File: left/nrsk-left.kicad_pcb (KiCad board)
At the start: 2 copper layers, 172.6 x 133.6 mm, 137 parts, among them J1 PJ-320D, J2 USB-C, J3 OLED 128x32, SW1 Esc, SW10 1, SW11 2, SW12 3, SW13 4, SW14 5, SW15 6, SW16 16, SW17 Tab, SW18 Q, SW19 W, SW2 F1, SW20 E, SW21 R, SW22 T, SW23 23, SW24 Ctrl, SW25 A, SW26 S, SW27 D, SW28 F, SW29 G, SW3 F2, SW30 30, SW31 Shift, SW32 Z, SW33 X, SW34 C, SW35 V, SW36 B, SW37 37, SW38 Ctrl, SW39 Opt, SW4 F3, SW40 Cmd, SW41 Space, SW42 Space, SW43 Space, SW44 44, SW5 F4, SW6 F5, SW7 F6, SW8 8, SW9 `, U1 RP2040, U2 USBLC6-2SC6, U4 AP2112K-3.3, U5 W25Q128JVS, Y1 12MHz

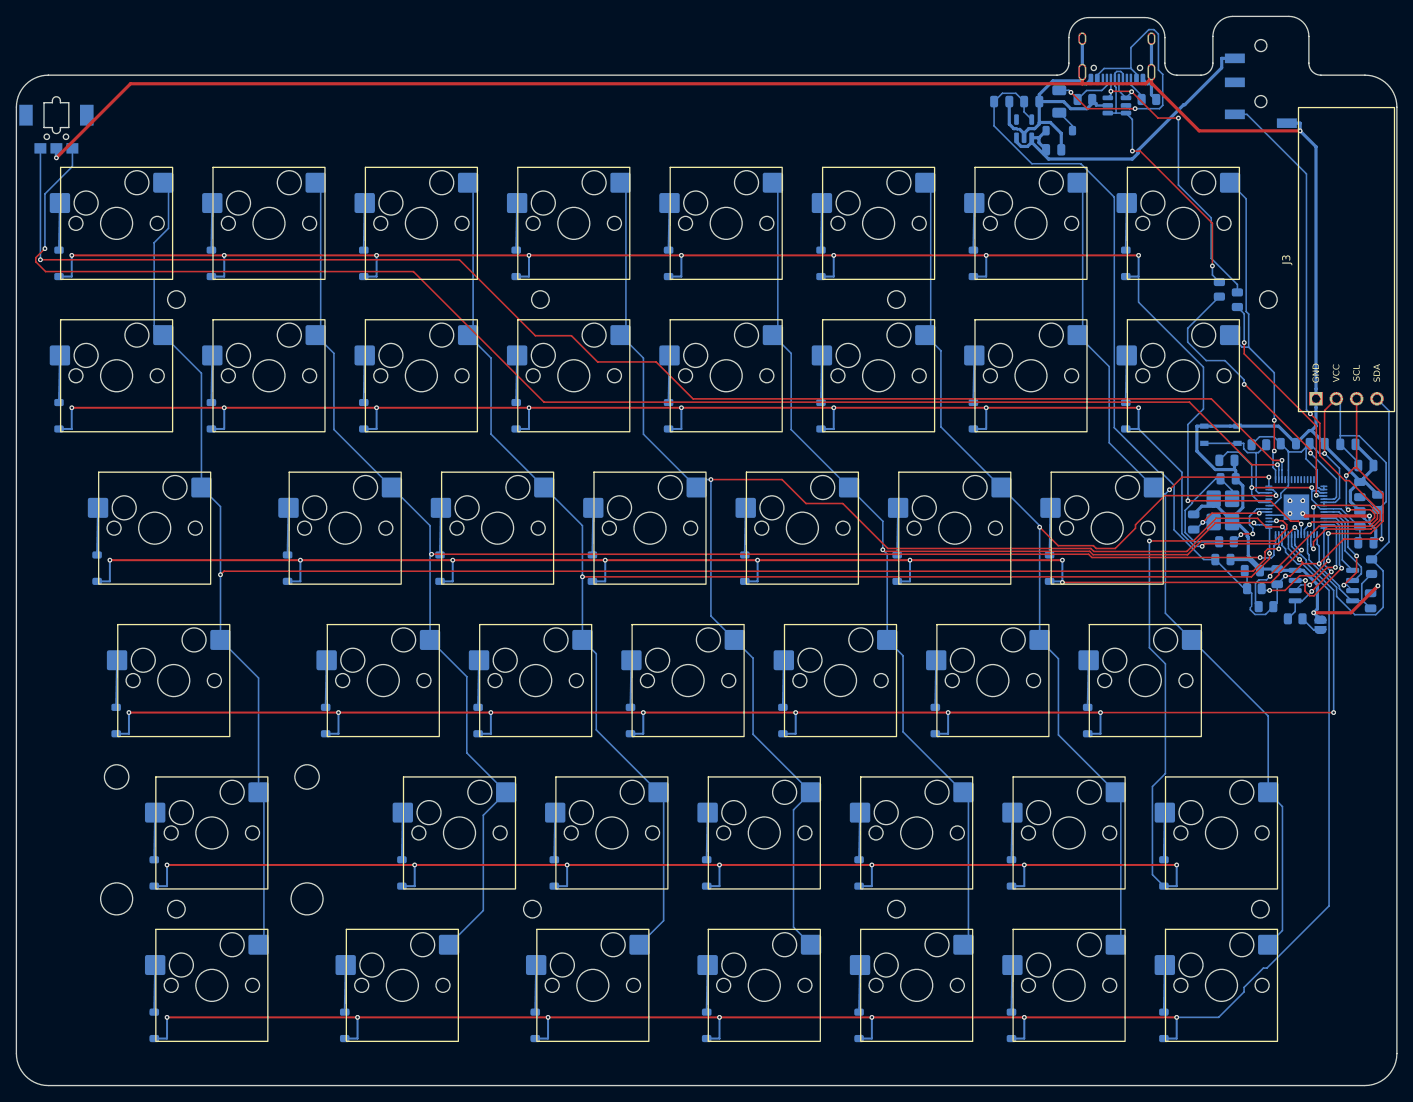
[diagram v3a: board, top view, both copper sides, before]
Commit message: GND copper on both faces of both boards, stitched with vias
- route.py pour(), run after routing and cleanup: a GND zone over the whole board on F.Cu and B.Cu
  (0.3 mm to other nets, 0.25 mm minimum width; the mounting-hole keepouts still win). The routed
  GND tracks stay. SMD pads join solidly (JLC reflows them), through-hole pads get thermal spokes,
  except the USB-C shell legs (JLC solders them; solid to GND)
- Stitching vias (0.6 / 0.3 mm) on a 5 mm grid, plus a 1.25 mm grid wherever no via is within
  3.75 mm, so narrow copper boxed in by tracks gets one too; a via goes only where its ring lies in
  the copper of both faces and its drill keeps 0.5 mm from other holes. Islands still unconnected are
  removed, with any via standing in them. Left 850, right ~966 stitching vias
- Applied to the routed boards (placement and routing unchanged, so the JLC CPL is unchanged);
  future builds pour after each routing pass
- DRC: 5 per side (silk at the connector mouths), down from 8: the 3 RP2040 thermal-pad vias now
  reach the F.Cu copper. 0 unconnected, 0 parity issues, ERC 0. Gerbers, PDFs, 3D viewer, assembly
  guide and board images regenerated
- README: board spec, how the copper is poured, DRC note

Co-Authored-By: Claude Opus 5.5 <noreply@anthropic.com>
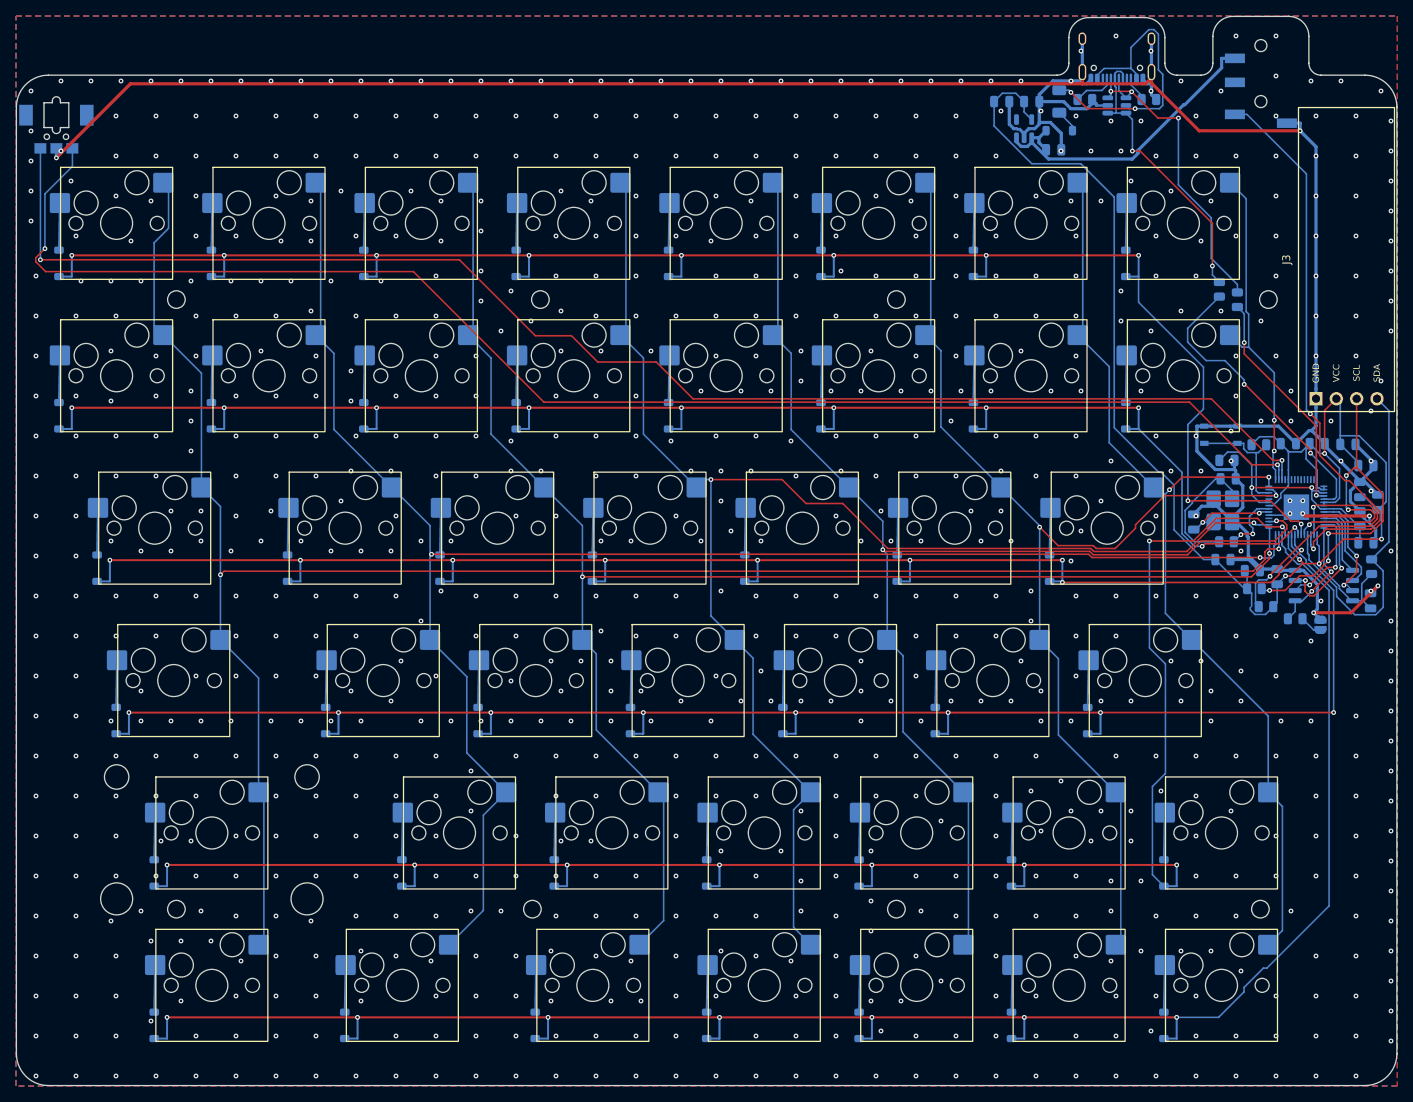
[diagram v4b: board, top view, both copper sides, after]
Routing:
- net GND: vias 9 -> 859
- added copper zone on B.Cu, net GND
- added copper zone on F.Cu, net GND

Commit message: Split link over USB-C instead of TRRS, so both port openings line up
The TRRS jack (PJ-320D) hung 5.0 mm under the PCB with its axis 2.5 mm down,
while the USB-C shell's axis is 1.63 mm down, so the two openings in the back
wall sat at different heights. The link now uses a second HRO TYPE-C-31-M-12:
same part, same height, same rounded slot.

- J1 is a USB-C receptacle: VBUS = VCC, D+ (A6/B6) = DATA (GP1), GND; D- and
  CC open, so a host or charger plugged in by mistake keeps VBUS off.
- PCB / case / JLC / BOM generators: the 'trrs' connector kind becomes 'link'
  and is handled like the host USB-C; PJ-320D footprint, model and JLC fix go.
- BOM: 4 USB-C receptacles, a C-C data cable for the link; one fewer
  Extended JLC part (9).
- Docs: README, ordering, pre-order checklist, thumbwheel check, assembly
  guide updated (pinout, which port is which, data cable required).
- Rebuilt: schematics, PCBs (0 unconnected, 0 parity issues, 4 silk warnings
  per side), fab outputs, case, BOM, JLC files, KiCad doc images.

Co-Authored-By: Claude Opus 5.5 <noreply@anthropic.com>
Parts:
- J1: value PJ-320D -> USB-C; footprint Connector_Audio:Jack_3.5mm_PJ320D_Horizontal -> Connector_USB:USB_C_Receptacle_HRO_TYPE-C-31-M-12
- moved J1 4.58 mm to (182.6, 17.5), turned to 0 degrees
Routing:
- net /SCL: track 57.6 -> 34.2 mm, vias 6 -> 2
- net /ROW3: track 204.8 -> 186.4 mm
- net /3V3: track 207.2 -> 192.5 mm
- net /SDA: track 44.6 -> 30.8 mm, vias 0 -> 2
- net /VBUS: track 38.5 -> 25.2 mm, vias 2 -> 3
- net /D-: track 28.6 -> 41.3 mm
- net /HAND: track 34.5 -> 23.5 mm, vias 2 -> 0
- net /ROW5: track 230.3 -> 240.9 mm, vias 7 -> 9
- net /VFUSE: track 2.93 -> 11.2 mm
- net /ROW0: track 216.2 -> 223.6 mm
- net VCC: track 39.9 -> 47.2 mm, vias 0 -> 2
- net /DATA: track 71.7 -> 78.5 mm
- net /COL4: track 161.2 -> 155.9 mm
- net /QSPI_SD0: track 8.89 -> 14.2 mm, vias 0 -> 2
- net /XIN: track 11.8 -> 17.0 mm
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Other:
- board size 172.6 x 133.6 mm -> 172.6 x 133.5 mm

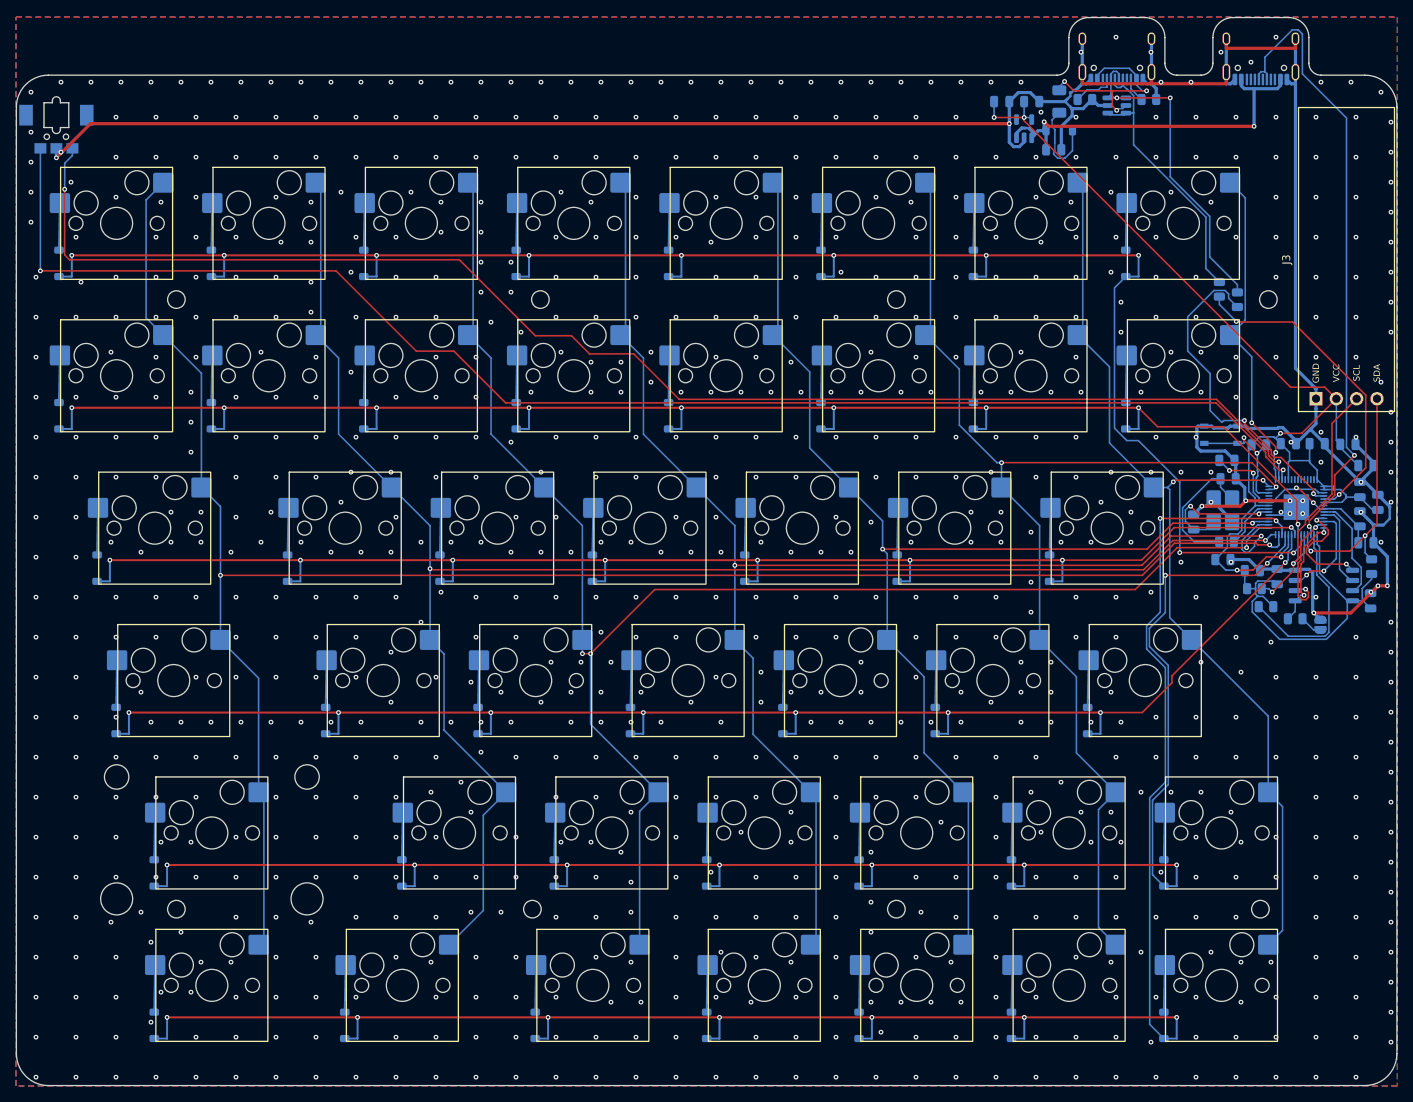
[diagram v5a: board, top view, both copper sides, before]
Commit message: Remove the blank inner key column on both halves; even plate band round the OLED cover
KLE: the unlabeled keys of the inner column go (left 8, 16, 23, 30, 37, 44; right 71, 73, 75, 77, 79, 81), so
the halves have 38 + 42 = 80 keys. The right "\" key now sits in its own row (row 2, col 7) and the remap goes;
the left's COL7 stays unconnected in the schematic.

The gap is closed: the right board moves its keys one unit in (key_shift +1 u, width -1 u). The left board is
sized from its row 0-1 keycaps: COVER_FRAME + the OLED cover (window + 5 mm each side) + COVER_FRAME, less the
case wall, so it narrows by 15.4 mm instead of a full unit.

The OLED's half-mirror cover is now laid out from the plate band round it: 3.5 mm to the case outline (top and
inner edge), to the nearest row 0-1 keycaps, and to the row-2 keycap line below, on both halves; the corner at the
case corner is concentric with it (R9), the others R2. The OLED stays at its height: its display glass, 3 mm
toward the module's top, lands at the cover's centre, and higher up the module would leave the board's rounded
corner and meet the link USB-C's shield pins. make_case checks the band against keycaps and the outline.

Sizes: boards 157.1 / 180.5 x 126.3 mm, cases 174.1 / 197.5 x 143.3 mm. The drum stays centred on Backspace.
Docs (README, ordering, pre-order checklist, drum spec coordinates) follow: 80 switches / sockets / diodes,
69 1 u keycaps, LCSC 85 switches and 90 sockets, trays fit a 220 mm bed.

Checked: ./build.sh -> left 0 unconnected (31 zero-length router stubs removed), right 0 unconnected, 0 parity
issues, ERC 0 / 0; DRC 4 silkscreen-at-board-edge warnings per side, as on main; make_case.py checks ok on both
halves (OLED band, drum dial); make_jlc: left 77, right 81 placements; textlint 0 on the edited docs.

Co-Authored-By: Claude Opus 5.5 <noreply@anthropic.com>
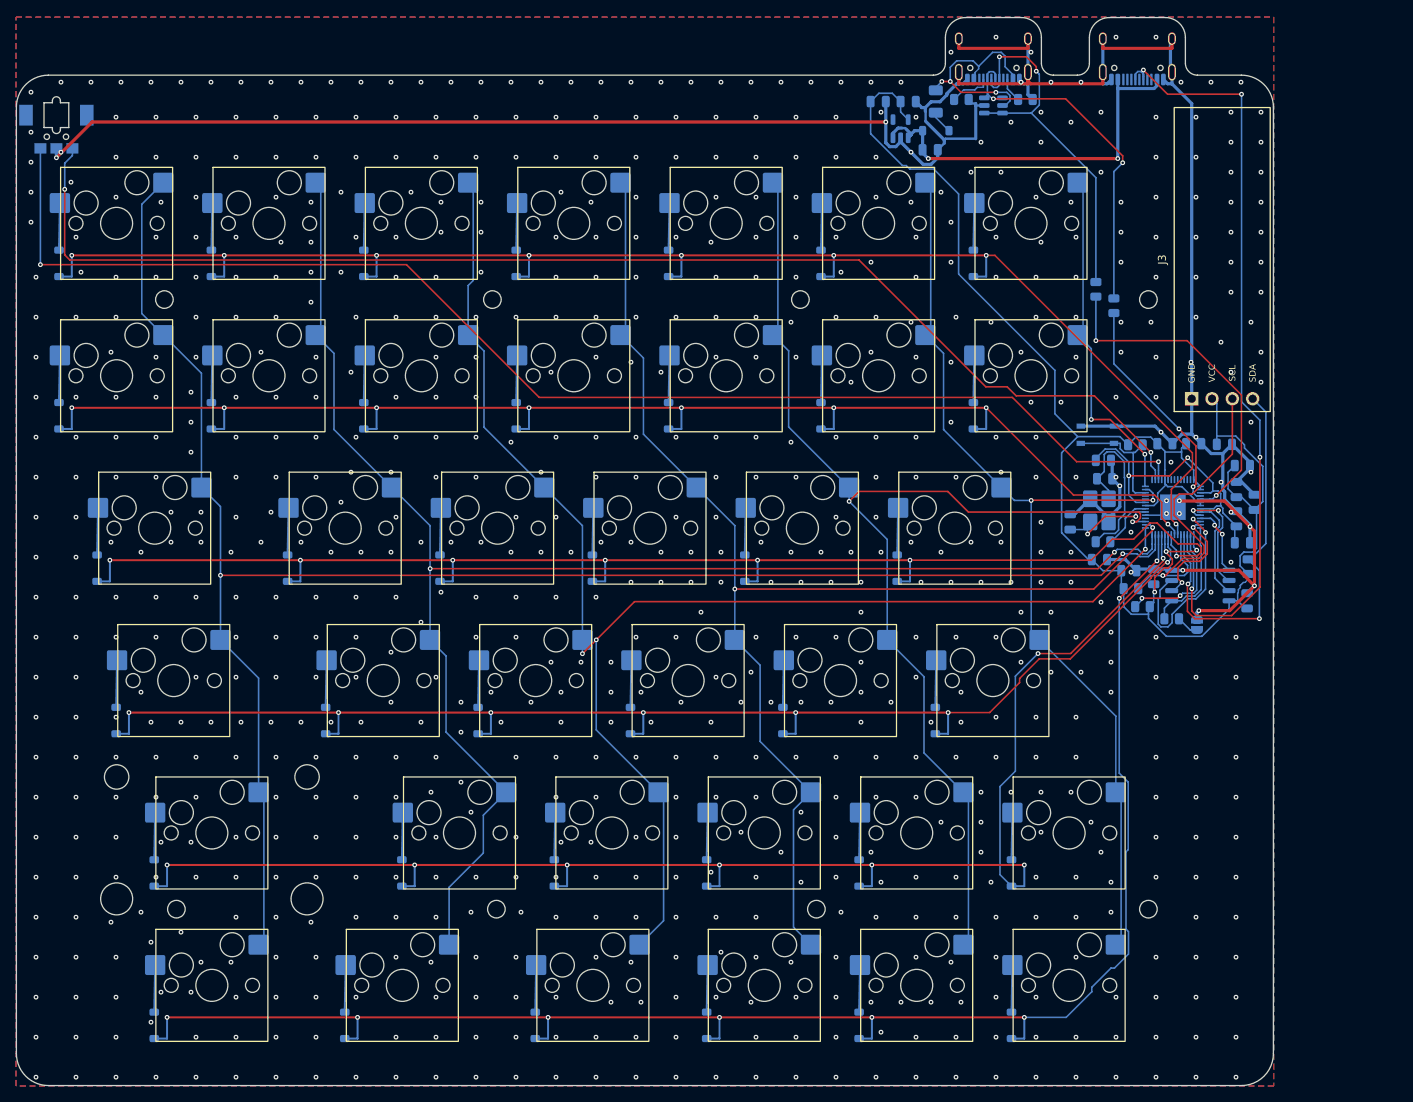
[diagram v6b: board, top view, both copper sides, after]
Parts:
- removed D39, D40, D41, D42, D43, D44: 1N4148W, Diode_SMD:D_SOD-123
- removed SW39: Opt, nrsk:SW_MX_Hotswap_1.25u
- removed SW40: Cmd, nrsk:SW_MX_Hotswap_1.25u
- removed SW41, SW42, SW43: Space, nrsk:SW_MX_Hotswap_1.00u
- removed SW44: 44, nrsk:SW_MX_Hotswap_1.00u
- SW10: value 1 -> 2
- SW11: value 2 -> 3
- SW12: value 3 -> 4
- SW13: value 4 -> 5
- SW14: value 5 -> 6
- SW15: value 6 -> Tab; footprint nrsk:SW_MX_Hotswap_1.00u -> nrsk:SW_MX_Hotswap_1.50u
- SW16: value 16 -> Q
- SW17: value Tab -> W; footprint nrsk:SW_MX_Hotswap_1.50u -> nrsk:SW_MX_Hotswap_1.00u
- SW18: value Q -> E
- SW19: value W -> R
- SW20: value E -> T
- SW21: value R -> Ctrl; footprint nrsk:SW_MX_Hotswap_1.00u -> nrsk:SW_MX_Hotswap_1.75u
- SW22: value T -> A
- SW23: value 23 -> S
- SW24: value Ctrl -> D; footprint nrsk:SW_MX_Hotswap_1.75u -> nrsk:SW_MX_Hotswap_1.00u
- SW25: value A -> F
- SW26: value S -> G
- SW27: value D -> Shift; footprint nrsk:SW_MX_Hotswap_1.00u -> nrsk:SW_MX_Hotswap_2.25u
- SW28: value F -> Z
- SW29: value G -> X
- SW30: value 30 -> C
- SW31: value Shift -> V; footprint nrsk:SW_MX_Hotswap_2.25u -> nrsk:SW_MX_Hotswap_1.00u
- SW32: value Z -> B
- SW33: value X -> Ctrl; footprint nrsk:SW_MX_Hotswap_1.00u -> nrsk:SW_MX_Hotswap_1.25u
- SW34: value C -> Opt; footprint nrsk:SW_MX_Hotswap_1.00u -> nrsk:SW_MX_Hotswap_1.25u
- SW35: value V -> Cmd; footprint nrsk:SW_MX_Hotswap_1.00u -> nrsk:SW_MX_Hotswap_1.25u
- SW36: value B -> Space
- SW37: value 37 -> Space
- SW38: value Ctrl -> Space; footprint nrsk:SW_MX_Hotswap_1.25u -> nrsk:SW_MX_Hotswap_1.00u
- SW8: value 8 -> `
- SW9: value ` -> 1
- moved D8 134.7 mm to (32.3, 63.6)
- moved SW8 134.7 mm to (39.5, 58.6)
- moved D15 111.2 mm to (37.1, 82.6)
- moved SW15 111.2 mm to (44.3, 77.6)
- moved SW38 107.2 mm to (158.6, 134.8)
- moved D38 107.2 mm to (151.4, 139.8)
- moved D16 106.5 mm to (60.9, 82.6)
- moved SW16 106.5 mm to (68.1, 77.6)
- moved D31 88.1 mm to (132.3, 120.7)
- moved SW31 88.1 mm to (139.5, 115.7)
- moved D21 80.9 mm to (39.5, 101.7)
- moved SW21 80.9 mm to (46.7, 96.7)
- moved SW32 76.2 mm to (158.6, 115.7)
- moved D32 76.2 mm to (151.4, 120.7)
- moved SW22 73.9 mm to (72.9, 96.7)
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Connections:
- D15 pad 1: /ROW1 -> /ROW2
- D16 pad 1: /ROW1 -> /ROW2
- D21 pad 1: /ROW2 -> /ROW3
- D22 pad 1: /ROW2 -> /ROW3
- D23 pad 1: /ROW2 -> /ROW3
- D27 pad 1: /ROW3 -> /ROW4
- D28 pad 1: /ROW3 -> /ROW4
- D29 pad 1: /ROW3 -> /ROW4
- D30 pad 1: /ROW3 -> /ROW4
- D33 pad 1: /ROW4 -> /ROW5
- D34 pad 1: /ROW4 -> /ROW5
- D35 pad 1: /ROW4 -> /ROW5
- D36 pad 1: /ROW4 -> /ROW5
- D37 pad 1: /ROW4 -> /ROW5
- D8 pad 1: /ROW0 -> /ROW1
- SW10 pad 1: /COL1 -> /COL2
- SW11 pad 1: /COL2 -> /COL3
- SW12 pad 1: /COL3 -> /COL4
- SW13 pad 1: /COL4 -> /COL5
- SW14 pad 1: /COL5 -> /COL6
- SW15 pad 1: /COL6 -> /COL0
- SW16 pad 1: /COL7 -> /COL1
- SW17 pad 1: /COL0 -> /COL2
- SW18 pad 1: /COL1 -> /COL3
- SW19 pad 1: /COL2 -> /COL4
- SW20 pad 1: /COL3 -> /COL5
- SW21 pad 1: /COL4 -> /COL0
- SW22 pad 1: /COL5 -> /COL1
- SW23 pad 1: /COL6 -> /COL2
- SW24 pad 1: /COL0 -> /COL3
- SW25 pad 1: /COL1 -> /COL4
- SW26 pad 1: /COL2 -> /COL5
- SW27 pad 1: /COL3 -> /COL0
- SW28 pad 1: /COL4 -> /COL1
- SW29 pad 1: /COL5 -> /COL2
- SW30 pad 1: /COL6 -> /COL3
- SW31 pad 1: /COL0 -> /COL4
- SW32 pad 1: /COL1 -> /COL5
- SW33 pad 1: /COL2 -> /COL0
- SW34 pad 1: /COL3 -> /COL1
- SW35 pad 1: /COL4 -> /COL2
- SW36 pad 1: /COL5 -> /COL3
- SW37 pad 1: /COL6 -> /COL4
- SW38 pad 1: /COL0 -> /COL5
- SW8 pad 1: /COL7 -> /COL0
- SW9 pad 1: /COL0 -> /COL1
- U1 pad 29: /COL7 -> unconnected-(U1-GPIO18-Pad29)
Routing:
- net /COL6: track 121.5 -> 43.4 mm
- net /COL7: track 41.2 -> 0.00 mm, vias 2 -> 0
- net /ROW5: track 240.9 -> 204.5 mm, vias 9 -> 8
- net /ROW0: track 223.6 -> 191.7 mm, vias 10 -> 8
- net /ROW4: track 215.9 -> 188.1 mm, vias 9 -> 8
- net /DATA: track 78.5 -> 99.7 mm, vias 2 -> 4
- net /ROW1: track 196.3 -> 175.6 mm, vias 9 -> 8
- net /COL5: track 144.4 -> 124.7 mm
- net /ROW3: track 186.4 -> 167.2 mm, vias 8 -> 7
- net /SDA: track 30.8 -> 49.3 mm
- net /COL3: track 182.4 -> 164.1 mm
- net /ENC_B: track 182.6 -> 166.7 mm
- net /ENC_A: track 178.7 -> 163.4 mm
- net /COL0: track 238.1 -> 223.3 mm
- net /COL1: track 216.2 -> 202.1 mm
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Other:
- board size 172.6 x 133.5 mm -> 157.1 x 133.5 mm
